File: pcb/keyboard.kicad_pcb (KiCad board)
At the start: 2 copper layers, 440 x 180 mm, 453 parts, among them J1 DC-005, J2 TYPE-C-31-M-12, J3 Touchscreen, J4 Touchscreen, M1 Motor_Servo, M10 Motor_Servo, M2 Motor_Servo, M3 Motor_Servo, M4 Motor_Servo, M5 Motor_Servo, M6 Motor_Servo, M7 Motor_Servo, M8 Motor_Servo, M9 Motor_Servo, SW1 Esc, SW10 F9, SW100 Enter, SW101 RotaryEncoder, SW11 F10, SW12 F11, SW13 F12, SW14 DEL, SW15 HOME, SW16 END, SW17 PGUP, SW18 PGDN, SW19 INS, SW2 F1, SW20 TILDE, SW21 1, SW22 2, SW23 3, SW24 4, SW25 5, SW26 6, SW27 7, SW28 8, SW29 9, SW3 F2, SW30 0, SW31 -, SW32 =, SW33 BKSP, SW34 Num, SW35 /, SW36 *, SW37 -, SW38 Tab, SW39 Q, SW4 F3, SW40 W, SW41 E, SW42 R, SW43 T, SW44 Y, SW45 U, SW46 I, SW47 O, SW48 P, SW49 [, SW5 F4, SW50 ], SW51 \, SW52 7, SW53 8, SW54 9, SW55 Caps, SW56 A, SW57 S, SW58 D, SW59 F, SW6 F5, SW60 G, SW61 H, SW62 J, SW63 K, SW64 L, SW65 ;, SW66 ", SW67 Enter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

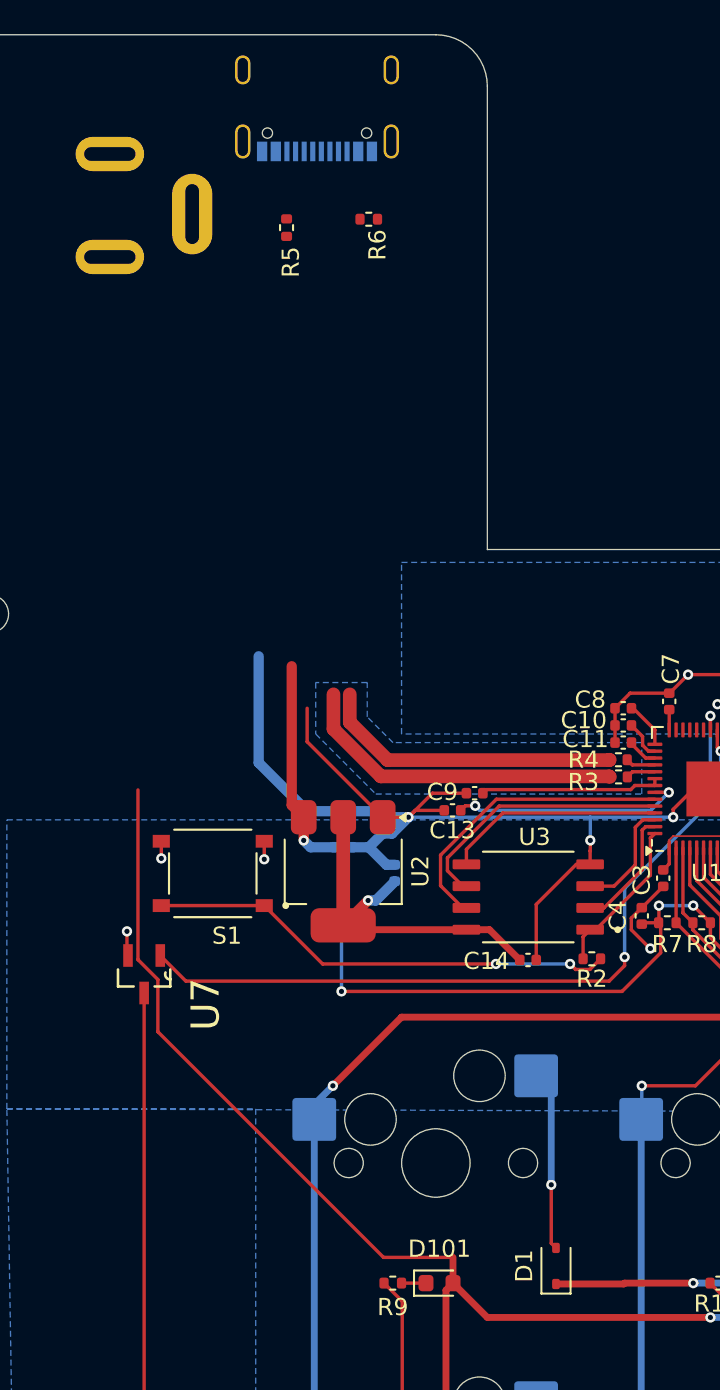
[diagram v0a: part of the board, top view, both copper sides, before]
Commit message: reroute power and usb :skull:
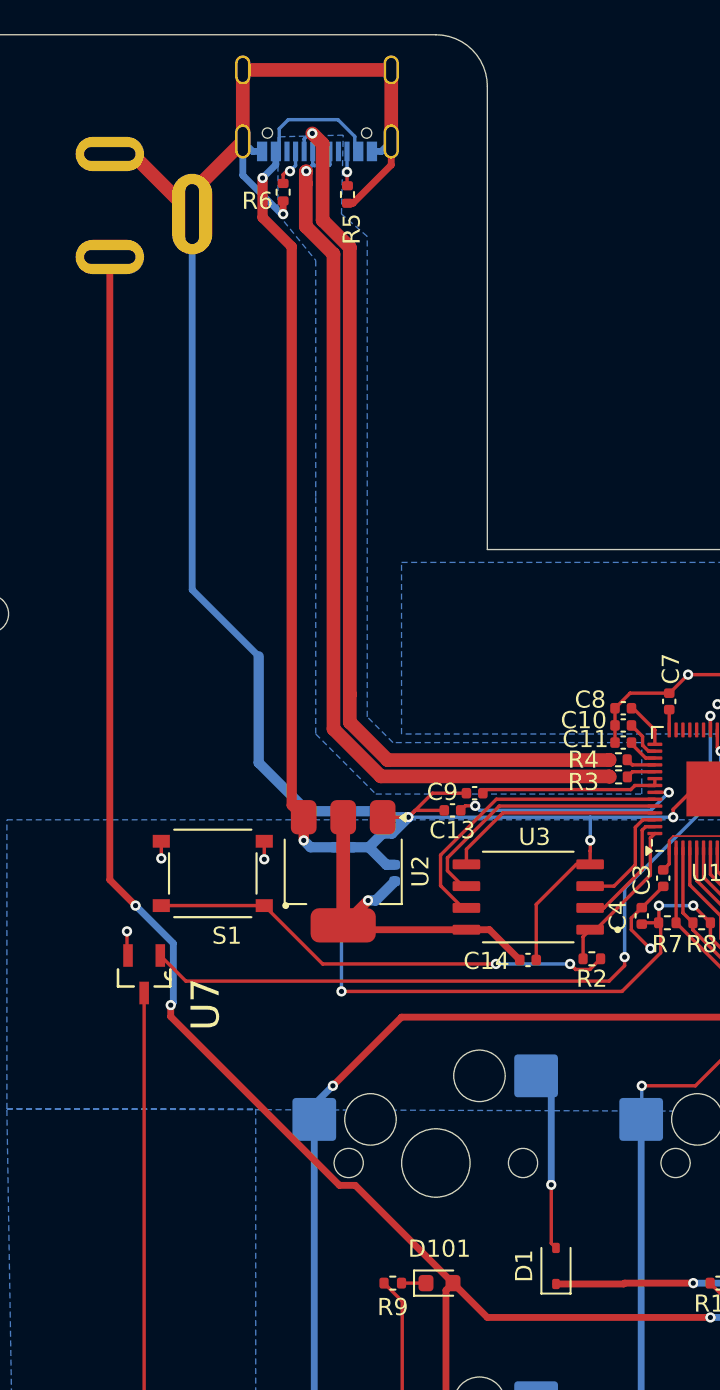
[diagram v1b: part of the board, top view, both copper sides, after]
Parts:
- moved R6 5.23 mm to (41.1, -6.58), turned to -90 degrees
- moved R5 4.04 mm to (44.9, -6.44)
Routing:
- net GND: track 204.3 -> 265.8 mm, vias 12 -> 13
- net VBUS: track 12.4 -> 50.8 mm, vias 1 -> 2
- net USB_D-: track 17.7 -> 54.1 mm, vias 0 -> 1
- net USB_D+: track 19.3 -> 53.6 mm, vias 0 -> 1
- net +5V: track 2507.1 -> 2537.1 mm, vias 45 -> 47
- net Net-(J2-CC1): track 0.00 -> 2.28 mm, vias 0 -> 1
- net Net-(J2-CC2): track 0.00 -> 2.01 mm, vias 0 -> 1
